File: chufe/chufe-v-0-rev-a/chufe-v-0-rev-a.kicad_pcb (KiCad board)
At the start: 2 copper layers, 200 x 50 mm, 22 parts, among them J1 Conn_02x08_Odd_Even, J2 Conn_02x08_Odd_Even, J3 Conn_02x08_Odd_Even, J4 Conn_02x08_Odd_Even, J5 Conn_02x08_Odd_Even, J6 Barrel_Jack_Switch, Q1 AO3401A, U1 URA2412YMD-20WR3_C5369773, U2 L7805

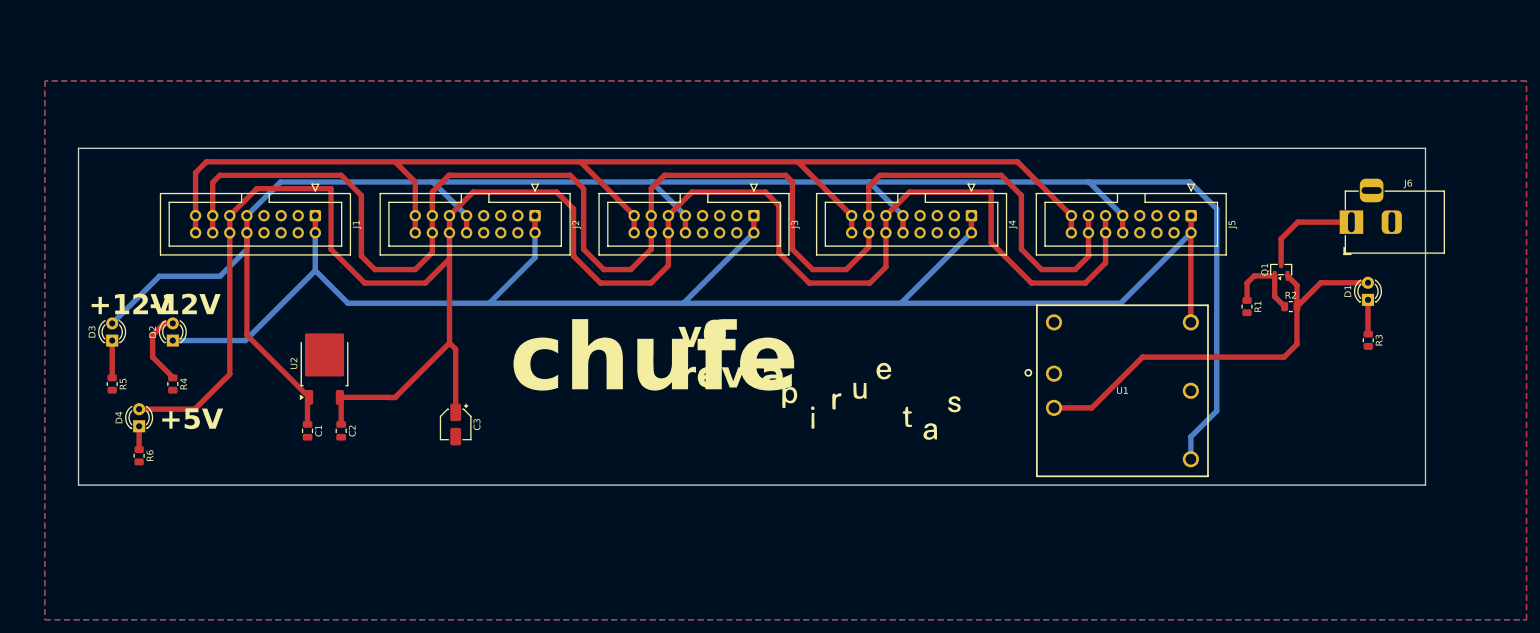
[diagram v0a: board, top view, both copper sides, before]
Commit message: agregar borrador pcb chufe
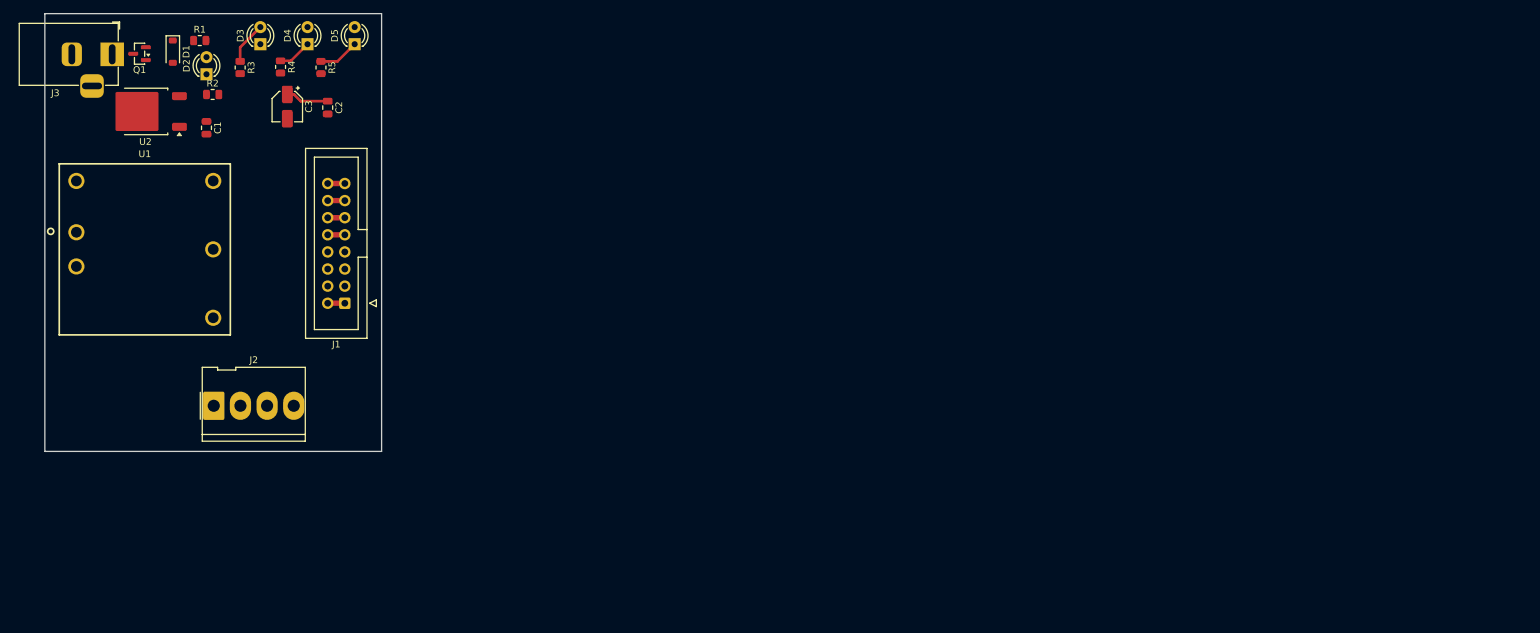
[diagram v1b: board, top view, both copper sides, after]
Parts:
- removed J4, J5: Conn_02x08_Odd_Even, Connector_IDC:IDC-Header_2x08_P2.54mm_Vertical
- removed J6: Barrel_Jack_Switch, Connector_BarrelJack:BarrelJack_Horizontal
- removed R6: 2k2, Resistor_SMD:R_0805_2012Metric
- added D5: LED, LED_THT:LED_D3.0mm, F.Cu at (66.0, 24.5)
- D1: value LED -> BZT52C5V6; footprint LED_THT:LED_D3.0mm -> Diode_SMD:D_SOD-123
- J2: value Conn_02x08_Odd_Even -> Conn_01x04_Pin; footprint Connector_IDC:IDC-Header_2x08_P2.54mm_Vertical -> Connector_Molex:Molex_KK-396_5273-04A_1x04_P3.96mm_Vertical
- J3: value Conn_02x08_Odd_Even -> Barrel_Jack_Switch; footprint Connector_IDC:IDC-Header_2x08_P2.54mm_Vertical -> Connector_BarrelJack:BarrelJack_Horizontal
- R1: value 2k2 -> 22k
- R2: value 1k -> 10k
- R5: value 10k -> 2k2
- moved D1 181.2 mm to (39.0, 25.6), turned to -90 degrees
- moved Q1 172.5 mm to (34.1, 25.9), turned to 180 degrees
- moved R3 172.3 mm to (49.0, 28.0)
- moved R2 163.2 mm to (44.9, 32.0)
- moved R1 160.4 mm to (43.0, 24.0), turned to 0 degrees
- moved U1 146.7 mm to (34.8, 55.0)
- moved J3 98.2 mm to (30.0, 26.0), turned to 0 degrees
- moved D4 62.0 mm to (59.0, 24.5)
- moved R5 56.3 mm to (61.0, 28.0)
- moved J2 55.4 mm to (45.1, 78.2), turned to 0 degrees
- moved C3 53.4 mm to (56.0, 33.8)
- moved R4 49.7 mm to (55.0, 27.9)
- moved D3 49.2 mm to (52.0, 24.5)
- moved C2 48.0 mm to (62.0, 34.0)
- moved C1 47.4 mm to (44.0, 37.0)
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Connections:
- D2 pad 1: -12V -> Net-(D2-K)
- D2 pad 2: Net-(D2-A) -> Net-(D1-K)
- D3 pad 1: Net-(D3-K) -> -12V
- D3 pad 2: +12V -> Net-(D3-A)
- D4 pad 2: +5V -> +12V
- J2 pad 2: -12V -> GND
- J2 pad 3: GND -> +5V
- J2 pad 4: GND -> +12V
- J3 pad 1: -12V -> Net-(Q1-D)
- J3 pad 2: -12V -> GND
- Q1 pad 1: Net-(Q1-G) -> Net-(D1-A)
- Q1 pad 2: Net-(D1-A) -> Net-(D1-K)
- R1 pad 1: Net-(Q1-G) -> Net-(D1-A)
- R2 pad 1: Net-(Q1-G) -> Net-(D2-K)
- R2 pad 2: Net-(D1-A) -> GND
- R3 pad 1: Net-(D1-K) -> Net-(D3-A)
- R4 pad 1: Net-(D2-A) -> Net-(D4-K)
- R5 pad 1: Net-(D3-K) -> Net-(D5-K)
- U1 pad 2: Net-(D1-A) -> Net-(D1-K)
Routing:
- net +5V: track 295.8 -> 8.95 mm
- net +12V: track 286.9 -> 3.64 mm
- net -12V: track 236.3 -> 2.54 mm
- net /CV: track 222.3 -> 2.54 mm
- net /GATE: track 185.0 -> 2.54 mm
- net Net-(D1-A): track 62.7 -> 0.00 mm
- net Net-(Q1-D): track 15.1 -> 0.00 mm
- net Net-(Q1-G): track 12.3 -> 0.00 mm
- net Net-(D2-A): track 11.3 -> 0.00 mm
- net Net-(D3-A): track 0.00 -> 6.33 mm
- net Net-(D5-K): track 0.00 -> 6.06 mm
- net Net-(D3-K): track 5.55 -> 0.00 mm
- net Net-(D1-K): track 5.10 -> 0.00 mm
- net Net-(D4-K): track 3.46 -> 5.02 mm
- removed copper zone on B.Cu, net GND
- removed copper zone on F.Cu, net GND
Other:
- board size 200 x 50 mm -> 50 x 65 mm
- board text removed: "+12V"
- board text removed: "+5V"
- board text removed: "-12V"
- board text removed: "chufe"
- board text removed: "rev-a"
- board text removed: "v0"

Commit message: añadida placa chufe
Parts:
- added H1: M3, MountingHole:MountingHole_3.2mm_M3, F.Cu at (65.0, 24.4)
- added H2: M3, MountingHole:MountingHole_3.2mm_M3, F.Cu at (65.0, 80.0)
- added H3: M3, MountingHole:MountingHole_3.2mm_M3, F.Cu at (25.0, 25.0)
- added H4: M3, MountingHole:MountingHole_3.2mm_M3, F.Cu at (25.0, 80.0)
- moved U2 21.5 mm to (52.1, 47.5), turned to 90 degrees
- moved C1 20.8 mm to (51.0, 56.5), turned to 180 degrees
- moved R2 10.7 mm to (36.4, 38.5)
- moved D2 9.96 mm to (36.0, 34.9)
- moved J3 8.64 mm to (29.2, 34.6)
- moved D3 8.59 mm to (44.2, 28.2)
- moved D4 8.59 mm to (51.2, 28.2)
- moved D5 8.59 mm to (58.2, 28.2)
- moved R3 8.59 mm to (41.2, 31.7)
- moved R4 8.59 mm to (47.2, 31.6)
- moved R5 8.59 mm to (53.2, 31.7)
- moved R1 7.81 mm to (37.1, 29.1), turned to -90 degrees
- moved C3 7.78 mm to (49.0, 37.2)
- moved C2 7.78 mm to (55.0, 37.4)
- moved D1 2.28 mm to (36.9, 24.8)
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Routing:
- net +12V: track 3.64 -> 84.6 mm, vias 0 -> 2
- net -12V: track 2.54 -> 80.1 mm
- net +5V: track 8.95 -> 84.7 mm
- net Net-(D1-K): track 0.00 -> 46.1 mm
- net Net-(D1-A): track 0.00 -> 15.3 mm, vias 0 -> 2
- net Net-(Q1-D): track 0.00 -> 10.3 mm
- net Net-(D2-K): track 0.00 -> 3.72 mm
- added copper zone on B.Cu, net GND
- added copper zone on F.Cu, net GND
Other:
- board text added: "-12"
- board text added: "12"
- board text added: "5"

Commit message: usar nueva github action
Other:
- board text added: "2026-10"
- board text added: "chufe"
- board text added: "rev a"
- board text added: "v0"
